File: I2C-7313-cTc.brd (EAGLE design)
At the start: 150 x 99.7 mm, 38 parts, among them CON1 CONNECTOR-I2CLEFT, IC1 MAX7313AEG, SW1 CTC-6PDT, SW2 CTC-4P3T

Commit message: 2.1-panel
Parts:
- added AD3, AD4, AD5, I2C-CABLE1: (no value), con-lstb:MA04-2
- added C4, C5: 0.1uF, SPCoast:0805-CAP
- added C6: 220uF, SPCoast:E5-10.5
- added CODEBUTTON1, MCLED1: (no value), SPCoast:1X02_LOCK
- added CON2: CONNECTOR-I2CLEFT, SPCoast:I2C-L
- added IC2: MAX7313AEG, maxim:QSOP24
- added LED-SIG-E1, LED-SIG-W1, LED-SW-N1: Green, SPCoast:LED3MM
- added LED-SIG-S1: Red, SPCoast:LED3MM
- added LED-SW-R1: Red/Orange, SPCoast:LED3MM
- added MCSWITCH1: (no value), SPCoast:SCREWTERMINAL-5MM-2
- added MODBOARDLEDS1: (no value), SPCoast:1X06_LOCK_LONGPADS
- added R17, R20, R22, R23, R24, R25: 82R, SPCoast:0805-RES
- added R18, R19, R21: 56R, SPCoast:0805-RES
- added R26, R27, R28, R29, R30, R31, R32: 10k, SPCoast:0805-RES
- added SW3: CTC-4P3T, SPCoast:CTC-4P3T
- added SW4: CTC-6PDT, SPCoast:CTC-6PDT-ROTARY
- added VR2: 3v3, SPCoast:SOT223
- BOARD1: value BOARD100X150X2-NOHOLES -> (none)
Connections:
- new net N$10: MCLED1.1, R22.2
- new net N$11: MODBOARDLEDS1.2, R23.2
- new net N$12: MODBOARDLEDS1.4, R24.2
- new net N$13: MODBOARDLEDS1.6, R25.2
- new net N$14: LED-SW-N1.K, R21.2
- new net N$15: LED-SW-R1.K, R20.2
- new net N$16: LED-SIG-E1.K, R19.2
- new net N$17: LED-SIG-W1.K, R18.2
- new net N$18: LED-SIG-S1.K, R17.2
- new net SCL1: AD3.8, AD4.8, AD5.8, CON2.SCL, CON2.SCL@1, I2C-CABLE1.1, I2C-CABLE1.2, IC2.22
- new net SDA1: AD3.6, AD4.6, AD5.6, CON2.SDA, CON2.SDA@1, I2C-CABLE1.3, I2C-CABLE1.4, IC2.23
- net +3V3: now also AD3.4, AD4.4, AD5.4, C5.1, IC2.24, LED-SIG-E1.A, LED-SIG-S1.A, LED-SIG-W1.A, LED-SW-N1.A, LED-SW-R1.A, MCLED1.2, R23.1, R24.1, R25.1, R26.1, R27.1, R28.1, R29.1, R30.1, R31.1, R32.1, VR2.2, VR2.4
- net +5V: now also C4.1, C6.+, CON2.V+, CON2.V+@1, I2C-CABLE1.5, I2C-CABLE1.6, VR2.3
- net AD0: now also AD3.1, AD3.3, AD3.5, AD3.7, IC2.21
- net AD1: now also AD4.1, AD4.3, AD4.5, AD4.7, IC2.2
- net AD2: now also AD5.1, AD5.3, AD5.5, AD5.7, IC2.3
- net CODE: now also CODEBUTTON1.1, IC2.17, R32.2
- net GND: now also AD3.2, AD4.2, AD5.2, C4.2, C5.2, C6.-, CODEBUTTON1.2, CON2.GND, CON2.GND@1, I2C-CABLE1.7, I2C-CABLE1.8, IC2.12, MCSWITCH1.2, SW3.A, SW4.A, VR2.1
- net LED-MC: now also IC2.13, R22.1
- net LED-SIG-E: now also IC2.18, R19.1
- net LED-SIG-S: now also IC2.19, R18.1
- net LED-SIG-W: now also IC2.20, R17.1
- net LED-SW-N: now also IC2.4, R20.1
- net LED-SW-R: now also IC2.5, R21.1
- net MB1: now also IC2.7, MODBOARDLEDS1.1
- net MB2: now also IC2.8, MODBOARDLEDS1.3
- net MB3: now also IC2.9, MODBOARDLEDS1.5
- net MC: now also IC2.6, MCSWITCH1.1, R26.2
- net SIG-E: now also IC2.16, R31.2, SW3.A1
- net SIG-S: now also IC2.15, R30.2, SW3.A2
- net SIG-W: now also IC2.14, R29.2, SW3.A3
- net SW-N: now also IC2.11, R28.2, SW4.A1
- net SW-R: now also IC2.10, R27.2, SW4.A2
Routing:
- net SDA1: track 0.00 -> 151.7 mm, vias 0 -> 1
- net SCL1: track 0.00 -> 147.8 mm, vias 0 -> 1
- net CODE: track 123.2 -> 246.3 mm, vias 3 -> 6
- net SIG-S: track 119.8 -> 239.5 mm, vias 2 -> 4
- net SIG-E: track 118.3 -> 236.6 mm, vias 2 -> 4
- net SIG-W: track 117.8 -> 235.5 mm, vias 2 -> 4
- net LED-MC: track 97.0 -> 194.1 mm, vias 2 -> 4
- net AD2: track 89.7 -> 179.3 mm, vias 1 -> 2
- net MB1: track 87.2 -> 174.4 mm
- net AD1: track 81.1 -> 162.1 mm, vias 1 -> 2
- net MB2: track 79.0 -> 157.9 mm
- net MB3: track 70.7 -> 141.4 mm
- net AD0: track 69.8 -> 139.7 mm, vias 1 -> 2
- net LED-SW-N: track 64.7 -> 129.5 mm
- net LED-SW-R: track 64.3 -> 128.5 mm
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
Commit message: normalized values
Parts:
- AD0, AD1, AD2, AD3, AD4, AD5, I2C-CABLE, I2C-CABLE1: value (none) -> 2x4-0.100
- BOARD1: value (none) -> BOARD
- CODEBUTTON, CODEBUTTON1, MCLED, MCLED1, MODBOARDLEDS, MODBOARDLEDS1: value (none) -> 0.100
- CON1, CON2: value CONNECTOR-I2CLEFT -> I2C
- MCSWITCH, MCSWITCH1: value (none) -> 0.200

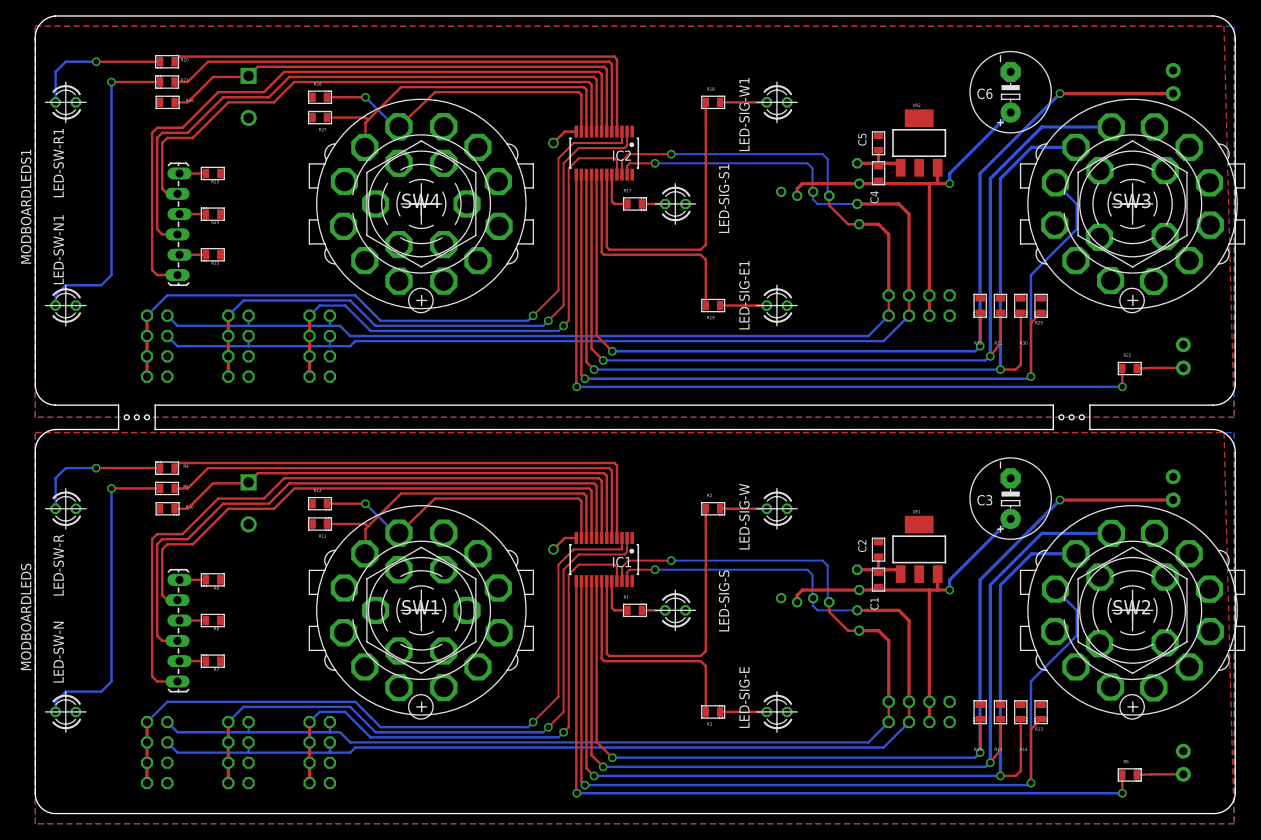
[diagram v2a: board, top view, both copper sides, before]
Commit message: replaced 4PDT rotary with 2P2T SR2616F-0202-18F58-D8-N
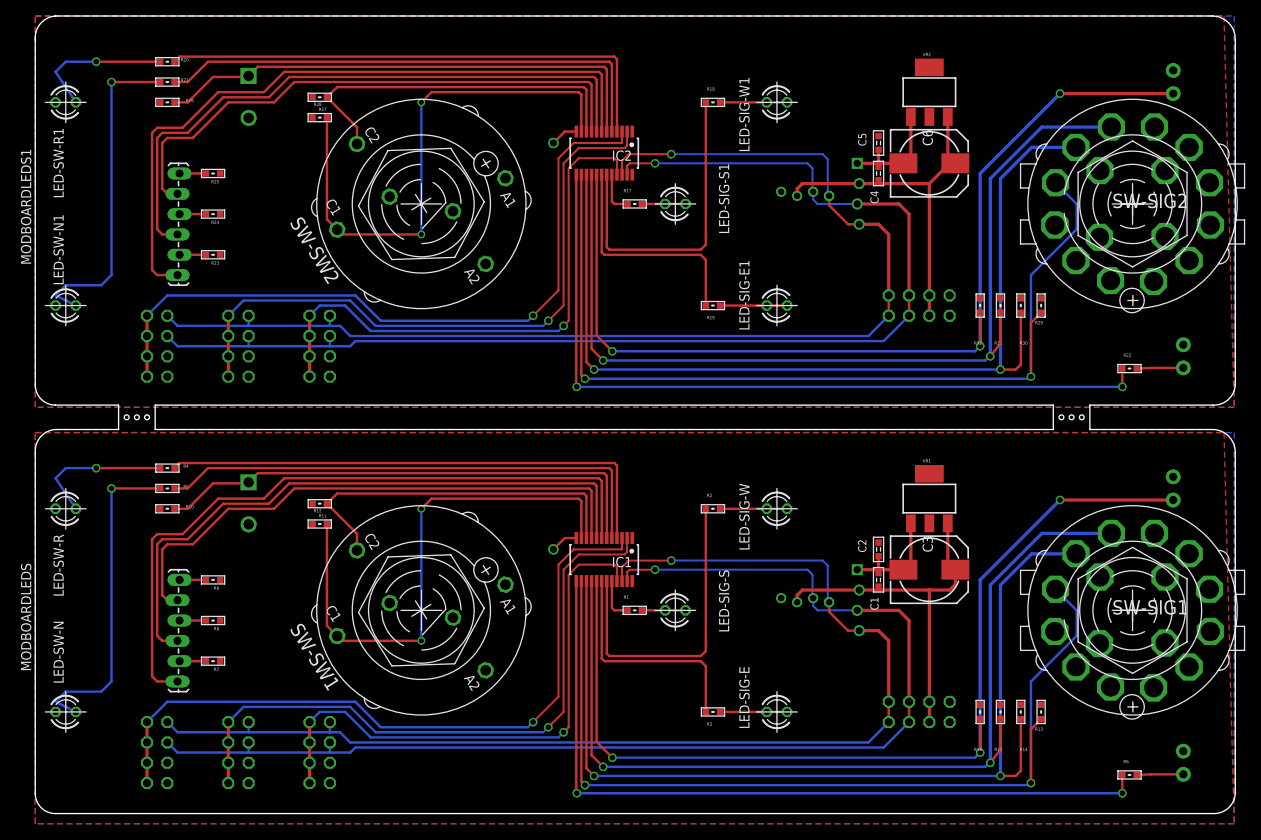
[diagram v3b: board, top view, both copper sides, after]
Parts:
- removed SW1, SW4: CTC-6PDT, SPCoast:CTC-6PDT-ROTARY
- added SW-SW1, SW-SW2: CK102X02, SPCoast:CK102X02
- C1, C2, C4, C5: device SPCoast:0805-CAP -> SPCoast:0603-CAP
- C3, C6: device SPCoast:E5-10.5 -> SPCoast:0810-CAP
- R1, R10, R11, R12, R13, R14, R15, R16, R17, R18, R19, R2, R20, R21, R22, R23, R24, R25, R26, R27, R28, R29, R3, R30, R31, R32, R4, R5, R6, R7, R8, R9: device SPCoast:0805-RES -> SPCoast:0603-RES
- moved C3 13.5 mm to (111.8, 30.5), turned to 0 degrees
- moved C6 13.5 mm to (111.8, 81.3), turned to 0 degrees
- moved VR2 6.48 mm to (111.8, 90.2)
- moved VR1 6.48 mm to (111.8, 39.4)
- moved R11 2.54 mm to (35.6, 38.7)
- moved R12 2.54 mm to (35.6, 36.2)
- moved R27 2.54 mm to (35.6, 89.5)
- moved R28 2.54 mm to (35.6, 87.0)
- renumbered SW2 to SW-SIG1, SW3 to SW-SIG2
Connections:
- net GND: now also SW-SW1.A, SW-SW1.C, SW-SW2.A, SW-SW2.C; no longer SW1.A, SW4.A
- net SW-N: now also SW-SW1.C1, SW-SW2.C1; no longer SW1.A1, SW4.A1
- net SW-R: now also SW-SW1.C2, SW-SW2.C2; no longer SW1.A2, SW4.A2
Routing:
- net SW-N: track 79.6 -> 134.2 mm, vias 2 -> 4
- net GND: track 22.2 -> 36.0 mm
- net +5V: track 102.2 -> 91.1 mm, vias 2 -> 0
- net SW-R: track 86.5 -> 91.5 mm
- net N$9: track 2.91 -> 5.45 mm
- net N$8: track 5.83 -> 8.37 mm
- net N$5: track 5.83 -> 8.37 mm
- net N$18: track 2.91 -> 5.45 mm
- net N$17: track 5.83 -> 8.37 mm
- net N$16: track 5.83 -> 8.37 mm
- net N$14: track 39.5 -> 41.1 mm
- net N$2: track 39.5 -> 41.1 mm
- net N$3: track 17.4 -> 18.2 mm
- net N$15: track 17.4 -> 18.2 mm
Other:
- board text added: "2016.05 2017.11 2020.11"
- board text added: "v2.2"
- board text removed: "John Plocher 2017-11"
- board text removed: "v2.1"
